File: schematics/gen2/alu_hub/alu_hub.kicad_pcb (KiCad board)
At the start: 2 copper layers, 100 x 91.1 mm, 22 parts, among them U1 74LS574, U10 74LS02, U2 74LS245, U3 74LS02, U4 74LS181, U5 74LS181, U6 74LS574, U7 74LS245, U8 74LS245, U9 74LS02

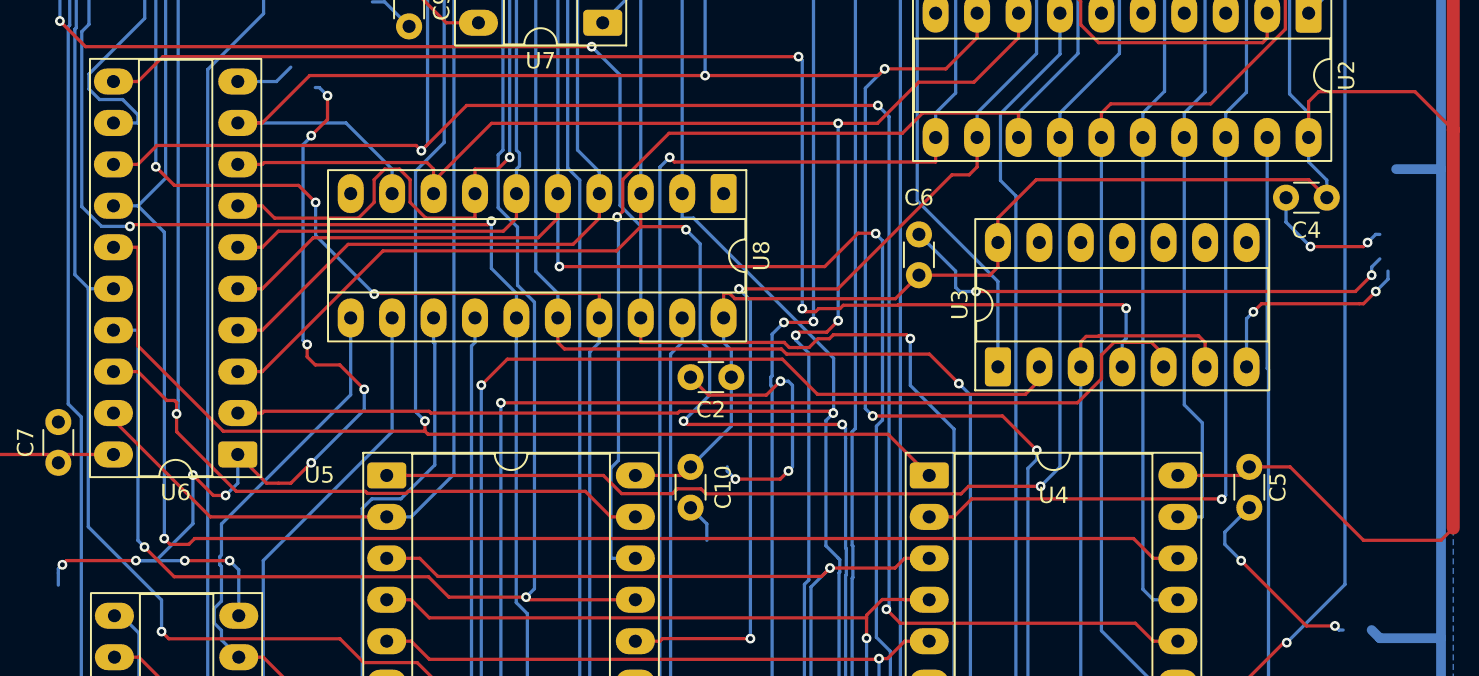
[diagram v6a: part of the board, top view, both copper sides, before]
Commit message: fix(alu): removed 90 degrees
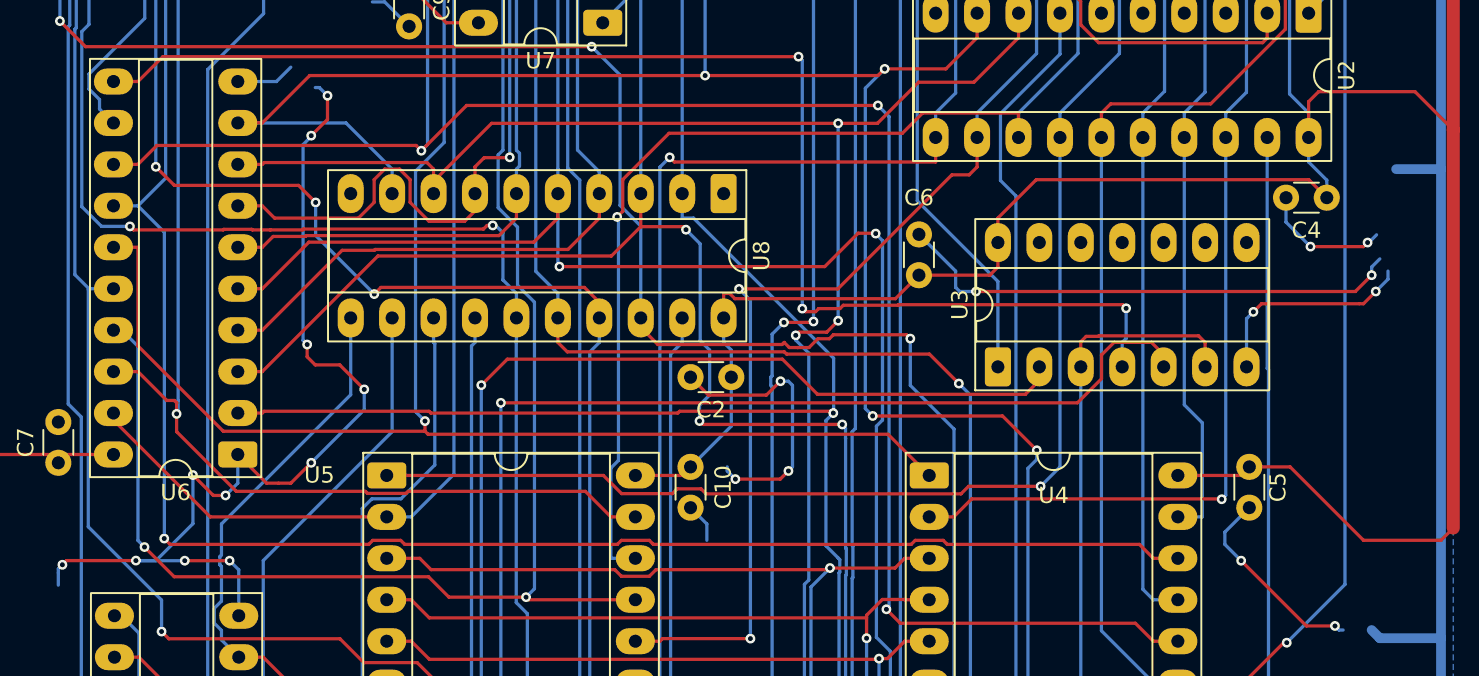
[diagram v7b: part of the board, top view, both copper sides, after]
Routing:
- net /LOW7: track 173.8 -> 170.9 mm
- net /DATA1: track 173.6 -> 172.2 mm
- net /LOW2: track 93.6 -> 93.1 mm

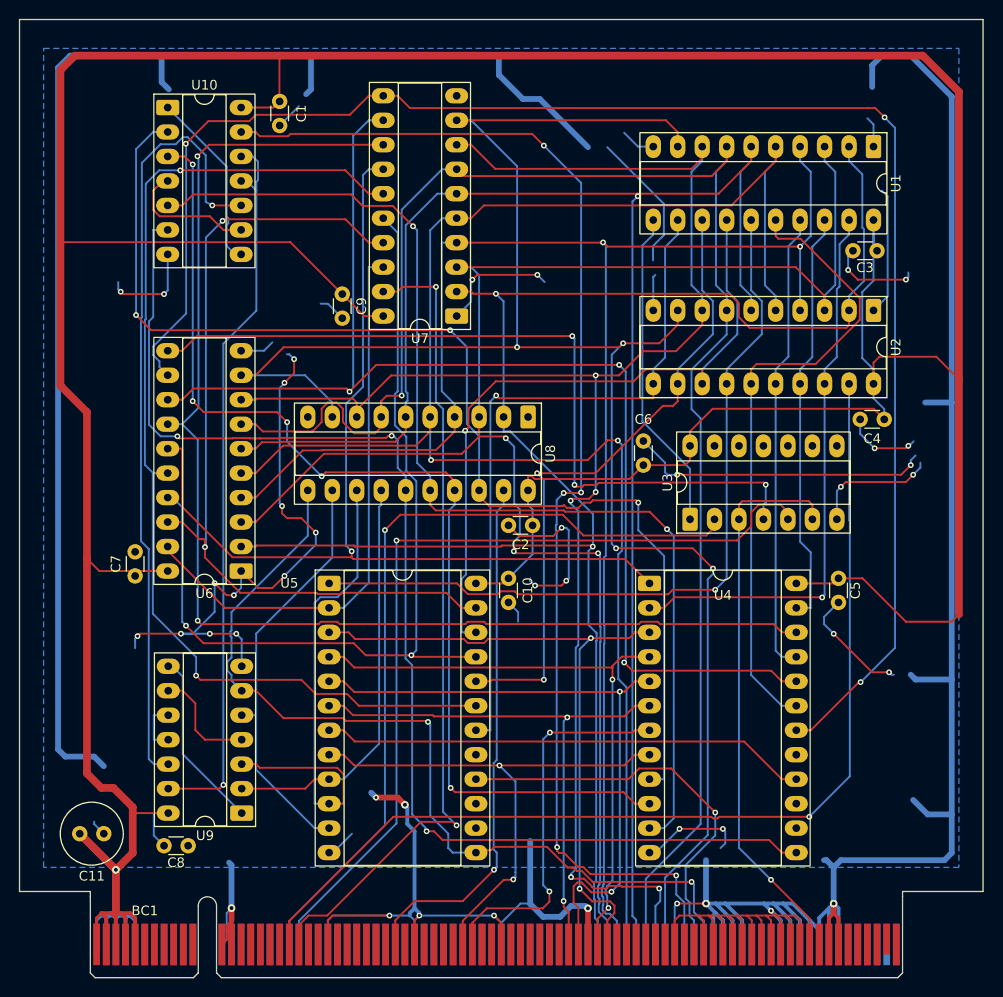
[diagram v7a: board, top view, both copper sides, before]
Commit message: feat(alu): add resistor symbol and connections to ALU hub schematic
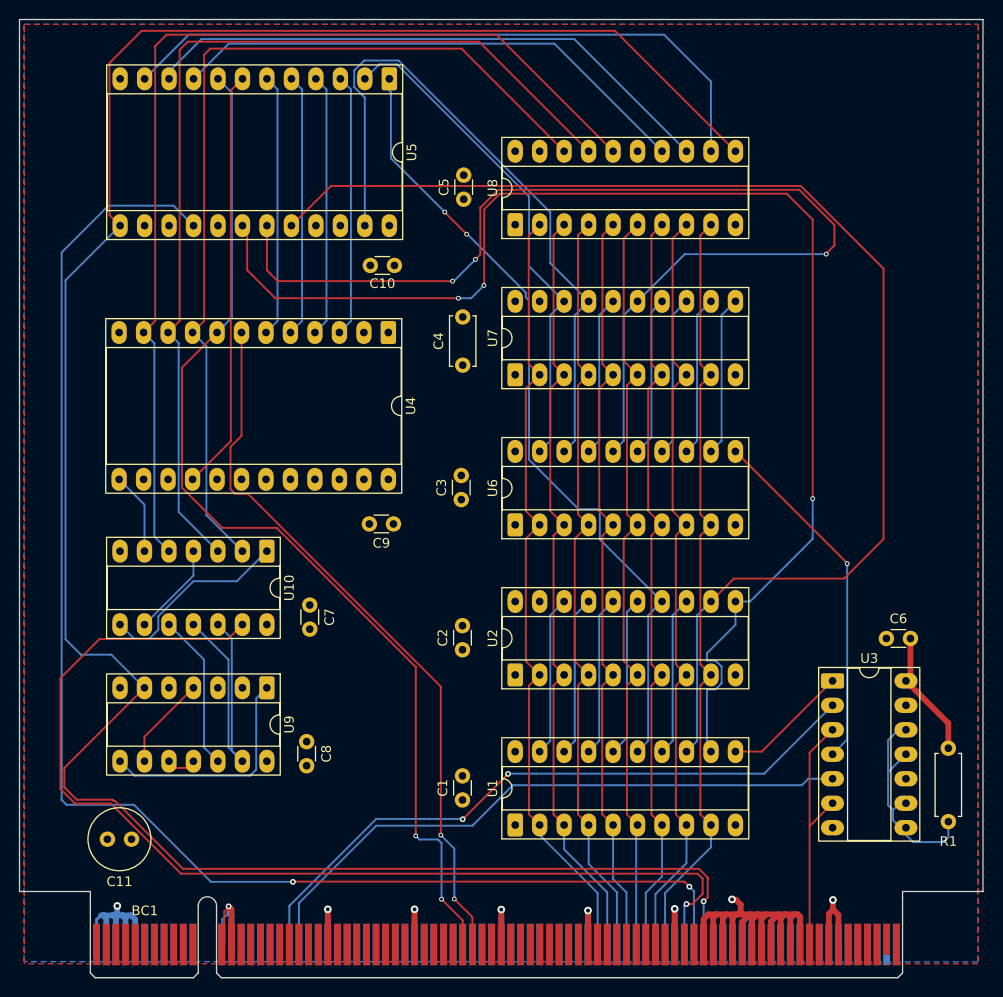
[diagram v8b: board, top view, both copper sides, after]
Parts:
- added R1: R, Resistor_THT:R_Axial_DIN0207_L6.3mm_D2.5mm_P7.62mm_Horizontal, F.Cu at (196.4, 120.1)
- C4: footprint Capacitor_THT:C_Disc_D3.0mm_W1.6mm_P2.50mm -> Capacitor_THT:C_Disc_D5.0mm_W2.5mm_P5.00mm
- moved U1 79.6 mm to (151.4, 128.1), turned to 90 degrees
- moved C1 72.5 mm to (146.0, 125.5)
- moved C5 57.1 mm to (146.1, 63.1)
- moved U2 53.1 mm to (151.4, 112.5), turned to 90 degrees
- moved U5 52.7 mm to (138.4, 50.7), turned to -90 degrees
- moved C3 48.2 mm to (145.8, 94.3), turned to 90 degrees
- moved U10 47.2 mm to (125.7, 99.7), turned to -90 degrees
- moved C4 41.6 mm to (146.0, 80.4), turned to 90 degrees
- moved C10 37.8 mm to (136.4, 70.0), turned to 0 degrees
- moved U4 37.6 mm to (138.3, 77.0), turned to -90 degrees
- moved C6 32.5 mm to (190.0, 108.7), turned to 0 degrees
- moved U6 28.8 mm to (151.4, 96.9), turned to 90 degrees
- moved U3 22.4 mm to (184.4, 113.1), turned to 0 degrees
- moved C9 21.5 mm to (136.3, 96.9), turned to 0 degrees
- moved U8 20.0 mm to (151.4, 65.8), turned to 90 degrees
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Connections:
- U3 pad 11: unconnected-(U3-Pad11) -> Net-(R1-Pad2)
- U3 pad 12: unconnected-(U3-Pad12) -> Net-(R1-Pad2)
- U3 pad 8: unconnected-(U3-Pad8) -> Net-(R1-Pad2)
- U3 pad 9: unconnected-(U3-Pad9) -> Net-(R1-Pad2)
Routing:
- net GND: track 782.9 -> 105.6 mm, vias 41 -> 8
- net VCC: track 473.1 -> 33.0 mm
- net /LOW7: track 170.9 -> 16.6 mm, vias 3 -> 0
- net Net-(BC1-ALUSO): track 94.2 -> 236.0 mm, vias 2 -> 1
- net Net-(U4-F3): track 129.8 -> 8.54 mm, vias 3 -> 0
- net /LOW5: track 134.1 -> 16.6 mm, vias 2 -> 0
- net /LOW6: track 129.0 -> 16.6 mm, vias 3 -> 0
- net Net-(BC1-~{RARGH}): track 107.7 -> 0.00 mm, vias 1 -> 0
- net /DATA7: track 187.1 -> 80.3 mm, vias 4 -> 0
- net Net-(BC1-~{ALUCO}): track 42.5 -> 148.5 mm, vias 1 -> 2
- net /DATA3: track 178.3 -> 79.2 mm, vias 2 -> 0
- net /DATA4: track 175.7 -> 79.0 mm, vias 1 -> 0
- net /DATA2: track 174.6 -> 79.8 mm, vias 2 -> 0
- net /DATA1: track 172.2 -> 80.5 mm, vias 3 -> 0
- net /DATA6: track 171.7 -> 80.2 mm, vias 5 -> 0
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- added copper zone on F.Cu, net VCC
